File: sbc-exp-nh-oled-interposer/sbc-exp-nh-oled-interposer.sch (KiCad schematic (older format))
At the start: 2 parts, among them J1 P, J2 NH OLED

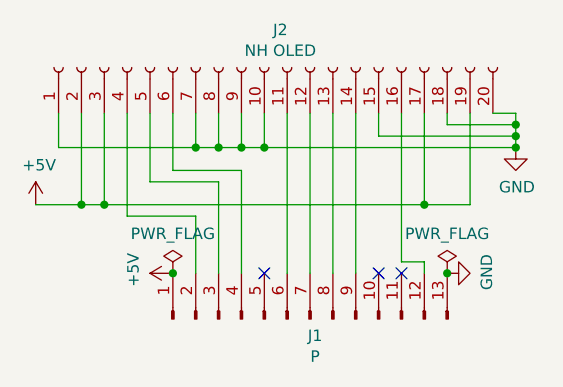
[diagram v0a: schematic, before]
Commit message: SBC v2.0
Changes:

 - Second VIA
 - NMI button (hardware debounced)
 - 5 status LEDs (power and each VIA port)
 - Ground and power planes
 - Smaller footprint RAM and oscillator
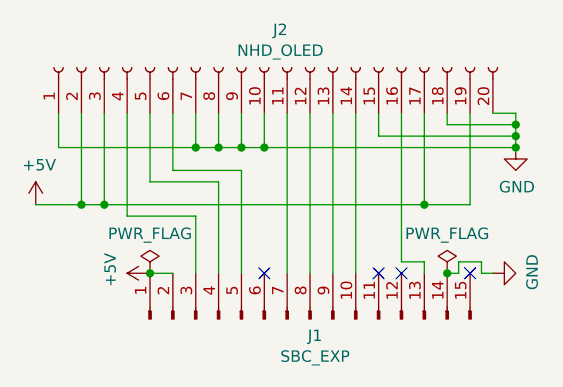
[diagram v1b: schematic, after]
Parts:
- removed J1: P, pin_header:PinHeader_1x13_P2.54mm_Vertical, symbol connector:Conn_01x13_Male
- added J1: SBC_EXP, pin_header:PinHeader_1x15_P2.54mm_Vertical, symbol connector:Conn_01x15_Male
- J2: value NH OLED -> NHD_OLED
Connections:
- net +5V: now also J1.1 (Pin_1), J1.2 (Pin_2)
- net GND: now also J1.14 (Pin_14)
- net at J2.11 (Pin_11): now also J1.7 (Pin_7)
- net at J2.12 (Pin_12): now also J1.8 (Pin_8)
- net at J2.13 (Pin_13): now also J1.9 (Pin_9)
- net at J2.14 (Pin_14): now also J1.10 (Pin_10)
- net at J2.16 (Pin_16): now also J1.13 (Pin_13)
- net at J2.4 (Pin_4): now also J1.3 (Pin_3)
- net at J2.5 (Pin_5): now also J1.4 (Pin_4)
- net at J2.6 (Pin_6): now also J1.5 (Pin_5)
- no-connect marks 3 -> 4
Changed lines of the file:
@@
 EESchema Schematic File Version 4
-LIBS:sbc-exp-nh-oled-interposer-cache
 EELAYER 30 0
 EELAYER END
@@
 Sheet 1 1
 Title "6502 SBC Expansion - NHD 0420CW OLED Interposer"
-Date "2021-09-16"
-Rev "1.0"
+Date "2021-11-09"
+Rev "2.0"
 Comp ""
 Comment1 ""
@@
 P 5400 3350
 F 0 "J2" V 5565 3280 50  0000 C CNN
-F 1 "NH OLED" V 5474 3280 50  0000 C CNN
+F 1 "NHD_OLED" V 5474 3280 50  0000 C CNN
 F 2 "pin_socket:PinSocket_1x20_P2.54mm_Vertical" H 5400 3350 50  0001 C CNN
 F 3 "~" H 5400 3350 50  0001 C CNN
@@
 $EndComp
 $Comp
-L connector:Conn_01x13_Male J1
-U 1 1 61437C51
-P 5600 4450
-F 0 "J1" V 5527 4428 50  0000 C CNN
-F 1 "P" V 5436 4428 50  0000 C CNN
-F 2 "pin_header:PinHeader_1x13_P2.54mm_Vertical" H 5600 4450 50  0001 C CNN
-F 3 "~" H 5600 4450 50  0001 C CNN
-	1    5600 4450
-	0    -1   -1   0
-$EndComp
-$Comp
 L power:+5V #PWR0101
 U 1 1 6143AFF8
-P 5000 4250
-F 0 "#PWR0101" H 5000 4100 50  0001 C CNN
-F 1 "+5V" H 5015 4423 50  0000 C CNN
-F 2 "" H 5000 4250 50  0001 C CNN
-F 3 "" H 5000 4250 50  0001 C CNN
-	1    5000 4250
+P 4900 4250
+F 0 "#PWR0101" H 4900 4100 50  0001 C CNN
+F 1 "+5V" H 4915 4423 50  0000 C CNN
+F 2 "" H 4900 4250 50  0001 C CNN
+F 3 "" H 4900 4250 50  0001 C CNN
+	1    4900 4250
 	0    -1   -1   0
 $EndComp
@@
 L power:GND #PWR0102
 U 1 1 6143B3C5
-P 6200 4250
-F 0 "#PWR0102" H 6200 4000 50  0001 C CNN
-F 1 "GND" H 6205 4077 50  0000 C CNN
-F 2 "" H 6200 4250 50  0001 C CNN
-F 3 "" H 6200 4250 50  0001 C CNN
-	1    6200 4250
+P 6400 4250
+F 0 "#PWR0102" H 6400 4000 50  0001 C CNN
+F 1 "GND" H 6405 4077 50  0000 C CNN
+F 2 "" H 6400 4250 50  0001 C CNN
+F 3 "" H 6400 4250 50  0001 C CNN
+	1    6400 4250
 	0    -1   -1   0
 $EndComp
@@
 L power:PWR_FLAG #FLG0101
 U 1 1 6144A1D2
-P 5000 4250
-F 0 "#FLG0101" H 5000 4325 50  0001 C CNN
-F 1 "PWR_FLAG" H 5000 4423 50  0000 C CNN
-F 2 "" H 5000 4250 50  0001 C CNN
-F 3 "~" H 5000 4250 50  0001 C CNN
-	1    5000 4250
+P 4900 4250
+F 0 "#FLG0101" H 4900 4325 50  0001 C CNN
+F 1 "PWR_FLAG" H 4900 4423 50  0000 C CNN
+F 2 "" H 4900 4250 50  0001 C CNN
+F 3 "~" H 4900 4250 50  0001 C CNN
+	1    4900 4250
 	1    0    0    -1
 $EndComp
@@
 	1    0    0    -1
 $EndComp
-Connection ~ 5000 4250
-Connection ~ 6200 4250
 $Comp
 L power:GND #PWR0103
@@
 Wire Wire Line
 	6100 4200 6100 4250
+$Comp
+L connector:Conn_01x15_Male J1
+U 1 1 617C8B1A
+P 5600 4450
+F 0 "J1" V 5527 4428 50  0000 C CNN
+F 1 "SBC_EXP" V 5436 4428 50  0000 C CNN
+F 2 "pin_header:PinHeader_1x15_P2.54mm_Vertical" H 5600 4450 50  0001 C CNN
+F 3 "~" H 5600 4450 50  0001 C CNN
+	1    5600 4450
+	0    -1   -1   0
+$EndComp
+Connection ~ 4900 4250
+Wire Wire Line
+	5000 4250 4900 4250
+Wire Wire Line
+	6200 4250 6250 4250
+Wire Wire Line
+	6250 4250 6250 4200
+Wire Wire Line
+	6250 4200 6350 4200
+Wire Wire Line
+	6350 4200 6350 4250
+Wire Wire Line
+	6350 4250 6400 4250
+Connection ~ 6200 4250
+NoConn ~ 6300 4250
 $EndSCHEMATC
